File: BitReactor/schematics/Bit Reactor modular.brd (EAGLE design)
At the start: 100 x 50 mm, 111 parts, among them U1 ADC0808N, U2 4053D, U3 4053D, U4 741G3157DBVR, U5 TL072D, U6 LM3914N, U7 LM555D, U9 TL072D

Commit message: v1.2 from Ryan
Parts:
- removed JP1: (no value), jumper:JP1
- removed R66: 50k, Rebel:POT-ALPS-RK09L1140
- removed U9: TL072D, linear:SO08
- added C15, C16: 10u, resistor:E2-5
- added C17: 0.01uF, resistor:C0402
- added IC1: TL074D, linear:SO14
- C1, C8: device rcl:E5-6 -> resistor:E2-5
- C4: value 220pF -> 470pF
- R1, R16, R18, R2, R3, R4, R5, R6, R7, R8: value 2.26k -> 20k
- R10, R14, R15: value 1.13k -> 10k; device resistor:R0805W -> resistor:R0805
- R11, R12, R13, R9: value 1.13k -> 10k
- R17: value 2.26k -> 2.7K
- R19, R21, R22, R23: value 2.26k -> 10K; device resistor:R0805 -> Rebel:POT-ALPS-RK09L1140
- R20: value 2.26k -> 50k; device resistor:R0805 -> Rebel:POT-ALPS-RK09L1140
- R34: device resistor:R0402 -> resistor:R0805
- R36: value 10k -> 100k
- R54: value 120k -> 10k; device resistor:R0402 -> resistor:R0805
- R62, R63: value POT-ALPS-RK09L1140 -> 120K; device Rebel:POT-ALPS-RK09L1140 -> resistor:R0402
- R64, R65: value POT-ALPS-RK09L1140 -> 120k; device Rebel:POT-ALPS-RK09L1140 -> resistor:R0402
- moved R65 67.6 mm to (1.59, 30.3), turned to 0 degrees
- moved R63 61.5 mm to (7.78, 20.0), turned to 0 degrees
- moved R18 57.2 mm to (44.5, 43.8), turned to 0 degrees
- moved R19 40.9 mm to (49.7, 12.3)
- moved R21 37.4 mm to (68.8, 12.3)
- moved R64 33.6 mm to (58.3, 41.0), turned to 0 degrees
- moved R20 31.7 mm to (49.7, 37.7)
- moved R17 27.8 mm to (43.0, 3.97), turned to 270 degrees
- moved R22 18.2 mm to (87.8, 25.0)
- moved R13 17.6 mm to (87.8, 9.68), turned to 90 degrees
- moved C11 16.3 mm to (91.0, 42.7)
- moved C7 14.3 mm to (87.3, 1.59), turned to 180 degrees
- moved R41 10.3 mm to (1.27, 19.5), turned to 90 degrees
- moved R23 10.2 mm to (68.8, 37.7), turned to 270 degrees
- moved R12 9.24 mm to (87.8, 38.3), turned to 90 degrees
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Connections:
- removed net N$64: R14.2, R7.1, U2.14
- removed net N$67: R23.1, U4.1
- removed net N$74: R56.1, R63.2
- new net N$68: C16.+, R34.2
- new net N$85: R15.1, R16.1, U2.14
- net +12V: now also IC1.4, R17.2, R22.1; no longer R62.3, R64.3, U9.8
- net -12V: now also IC1.11; no longer U9.4
- net CV2IN: now also IC1.8; no longer U9.1
- net GND: now also C16.-, C17.1, IC1.10, IC1.12, IC1.3, IC1.5, R19.3, R21.1, R22.3, R23.1; no longer R17.2, R18.2, R19.2, R20.2, R21.2, R22.2, R23.2, R62.1, R63.1, R64.1, R65.1, U9.3, U9.5
- net N$10: now also AUDIOIN.P$2, C15.+; no longer R10.2, R3.1, U3.15
- net N$11: now also C15.-, R36.2; no longer R11.2, R4.1, U3.14
- net N$12: now also R13.1, R14.2, U2.1; no longer R12.2, R5.1
- net N$13: now also R5.1; no longer R12.1
- net N$14: now also R4.1; no longer R11.1
- net N$15: now also R3.1; no longer R10.1
- net N$16: now also R2.1; no longer R9.1
- net N$17: now also R8.1; no longer R15.1
- net N$18: now also R21.2, R62.1; no longer R15.2, R16.1, R8.1
- net N$19: now also IC1.2, R62.2, R63.1; no longer R17.1, U2.13
- net N$20: now also R18.2, R20.1, R34.1; no longer R34.2, R66.1
- net N$21: now also R7.1; no longer R14.1
- net N$22: now also R6.1; no longer R13.1
- net N$23: now also IC1.1, R56.1, R63.2; no longer R18.1, U2.1
- net N$24: now also R12.1, R13.2, U3.14; no longer R19.1
- net N$25: now also R11.1, R12.2, U3.15; no longer R20.1
- net N$26: now also R10.1, R11.2, U3.4; no longer R21.1
- net N$27: now also R10.2, R9.1, U4.4; no longer R22.1
- net N$28: now also R9.2, U4.1; no longer U4.4
- net N$38: now also R18.1; no longer R34.1
- net N$40: now also R20.2, R20.3; no longer R66.2, R66.3
- net N$42: now also R23.2, R64.2; no longer AUDIOIN.P$2, R36.2
- net N$45: now also U1.6; no longer JP1.2
- net N$47: now also IC1.6, R64.1; no longer R53.2
- net N$48: now also R23.3; no longer R65.3
- net N$49: now also IC1.7, R53.2, R65.1; no longer JP1.1, U1.6
- net N$65: now also R14.1, R15.2, U2.13; no longer R13.2, R6.1
- net N$71: now also IC1.13; no longer U9.6
- net N$72: now also R19.2; no longer R62.2
- net N$73: now also IC1.14; no longer U9.7
- net N$75: now also R21.3; no longer R63.3
- net N$80: now also C17.2
- net N$81: now also IC1.9; no longer U9.2
- net N$83: now also R22.2; no longer R64.2
- net N$9: now also R17.1, R19.1; no longer R2.1, R9.2, U3.4
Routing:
- net N$19: track 15.5 -> 96.4 mm, vias 0 -> 3
- net N$9: track 87.0 -> 11.7 mm, vias 4 -> 0
- net N$74: track 71.6 -> 0.00 mm, vias 1 -> 0
- net N$12: track 86.3 -> 21.5 mm, vias 3 -> 0
- net N$24: track 13.3 -> 53.8 mm, vias 0 -> 2
- net N$27: track 6.30 -> 40.3 mm, vias 0 -> 2
- net N$42: track 37.1 -> 4.34 mm, vias 1 -> 0
- net N$11: track 51.1 -> 20.7 mm, vias 2 -> 1
- net N$17: track 2.64 -> 31.3 mm, vias 0 -> 2
- net N$85: track 0.00 -> 28.4 mm
- net N$64: track 27.8 -> 0.00 mm
- net N$14: track 2.56 -> 27.4 mm
- net N$10: track 47.5 -> 24.0 mm, vias 2 -> 0
- net N$18: track 26.4 -> 3.29 mm
- net N$13: track 4.67 -> 24.4 mm
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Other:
- board text added: "C1"
- board text added: "C15"
- board text added: "C16"
- board text added: "C17"
- board text added: "C8"
- board text added: "D5"
- board text added: "R30"
- board text added: "R62"
- board text added: "R63"
- board text added: "R64"
- board text added: "R65"
- board text removed: "D6"

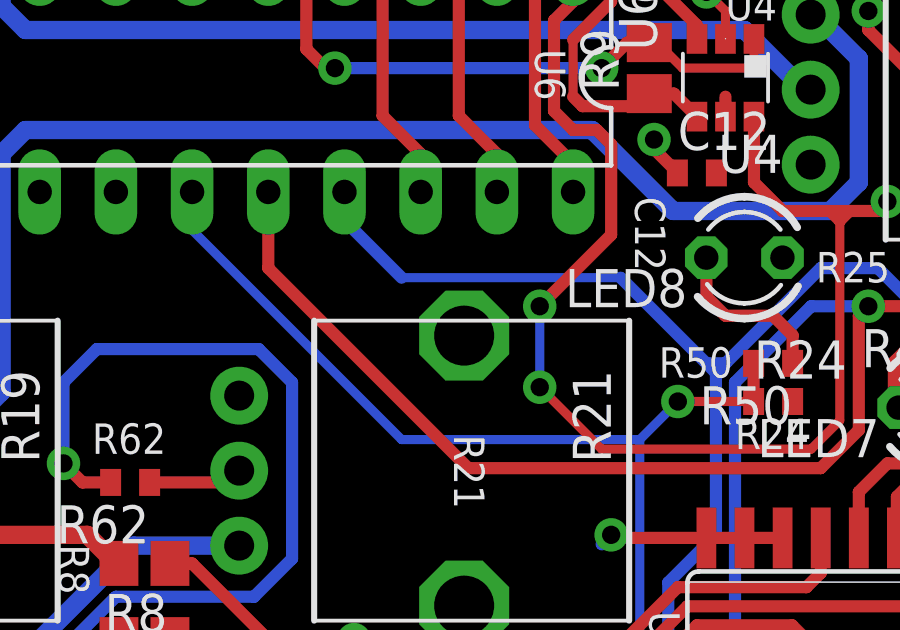
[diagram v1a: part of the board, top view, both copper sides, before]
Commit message: tied pot shells to gnd
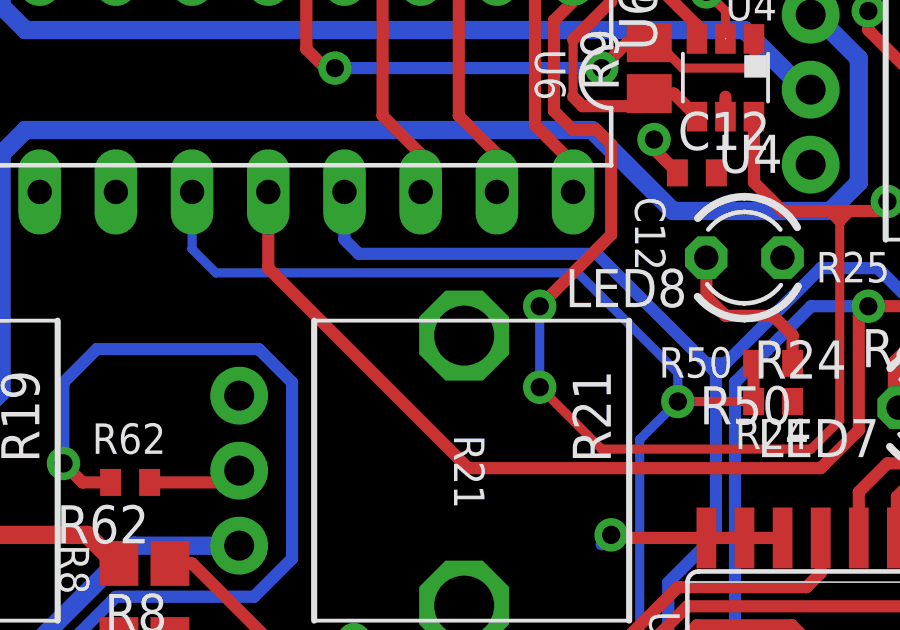
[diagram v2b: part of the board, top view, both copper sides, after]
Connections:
- net GND: now also R19.P$5, R19.P$6, R20.P$5, R20.P$6, R21.P$5, R21.P$6, R22.P$5, R22.P$6, R23.P$5, R23.P$6
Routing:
- net N$37: track 41.4 -> 43.1 mm
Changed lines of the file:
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@@
 <wire x1="2.68375" y1="20.47875" x2="2.69875" y2="20.47875" width="0.3048" layer="1"/>
 <wire x1="10.13" y1="26.05" x2="9.68375" y2="26.05" width="0.254" layer="1"/>
+<contactref element="R22" pad="P$5"/>
+<contactref element="R22" pad="P$6"/>
+<contactref element="R23" pad="P$5"/>
+<contactref element="R23" pad="P$6"/>
+<contactref element="R20" pad="P$5"/>
+<contactref element="R20" pad="P$6"/>
+<contactref element="R19" pad="P$5"/>
+<contactref element="R19" pad="P$6"/>
+<contactref element="R21" pad="P$5"/>
+<contactref element="R21" pad="P$6"/>
 </signal>
 <signal name="N$1">
@@
 <wire x1="77.1525" y1="10.16" x2="75.565" y2="8.5725" width="0.4064" layer="16"/>
 <wire x1="82.55" y1="19.05" x2="80.645" y2="19.05" width="0.4064" layer="16"/>
-<wire x1="64.77" y1="21.59" x2="64.77" y2="20.6375" width="0.4064" layer="16"/>
-<wire x1="64.77" y1="20.6375" x2="66.675" y2="18.7325" width="0.4064" layer="16"/>
-<wire x1="66.675" y1="18.7325" x2="73.9775" y2="18.7325" width="0.3048" layer="16"/>
-<wire x1="73.9775" y1="18.7325" x2="76.835" y2="15.875" width="0.4064" layer="16"/>
+<wire x1="73.18375" y1="19.52625" x2="76.835" y2="15.875" width="0.4064" layer="16"/>
 <wire x1="76.835" y1="15.875" x2="77.1525" y2="15.5575" width="0.4064" layer="16"/>
 <wire x1="76.835" y1="15.875" x2="77.47" y2="15.875" width="0.4064" layer="16"/>
+<wire x1="64.77" y1="21.59" x2="64.77" y2="20.0025" width="0.4064" layer="16"/>
+<wire x1="64.77" y1="20.0025" x2="65.24625" y2="19.52625" width="0.4064" layer="16"/>
+<wire x1="65.24625" y1="19.52625" x2="73.18375" y2="19.52625" width="0.4064" layer="16"/>
 </signal>
 <signal name="N$36">
@@
 <via x="75.8825" y="14.605" extent="1-16" drill="0.6096"/>
 <wire x1="75.8825" y1="14.605" x2="78.4075" y2="14.605" width="0.3048" layer="1"/>
-<wire x1="59.69" y1="21.59" x2="59.69" y2="20.32" width="0.3048" layer="16"/>
-<wire x1="59.69" y1="20.32" x2="66.675" y2="13.335" width="0.3048" layer="16"/>
-<wire x1="66.675" y1="13.335" x2="74.6125" y2="13.335" width="0.3048" layer="16"/>
 <wire x1="78.4075" y1="15.875" x2="78.4075" y2="14.62" width="0.4064" layer="1"/>
 <wire x1="78.4075" y1="14.62" x2="78.4225" y2="14.605" width="0.4064" layer="1"/>
 <wire x1="78.4075" y1="14.605" x2="78.4225" y2="14.605" width="0.4064" layer="1"/>
+<wire x1="59.69" y1="21.59" x2="59.69" y2="19.685" width="0.3048" layer="16"/>
+<wire x1="59.69" y1="19.685" x2="60.48375" y2="18.89125" width="0.3048" layer="16"/>
+<wire x1="60.48375" y1="18.89125" x2="72.54875" y2="18.89125" width="0.3048" layer="16"/>
+<wire x1="72.54875" y1="18.89125" x2="75.8825" y2="15.5575" width="0.3048" layer="16"/>
+<wire x1="75.8825" y1="15.5575" x2="75.8825" y2="14.605" width="0.3048" layer="16"/>
 </signal>
 <signal name="Y">

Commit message: v1.3
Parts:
- added C18: 10u, resistor:E2-5
- R17: value 2.7K -> 3.3K
- moved D1 0.95 mm to (24.1, 5.40)
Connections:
- net GND: now also C18.-
- net N$51: now also C18.+
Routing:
- net N$51: track 27.2 -> 29.8 mm
- net GND: track 129.7 -> 132.0 mm
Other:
- board text added: "Bit Reactor v1.3"
- board text added: "C18"
- board text added: "Rebel Technology"
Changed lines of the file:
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@@
 <?xml version="1.0" encoding="utf-8"?>
 <!DOCTYPE eagle SYSTEM "eagle.dtd">
-<eagle version="6.1">
+<eagle version="6.5.0">
 <drawing>
 <settings>
@@
 <setting verticaltext="up"/>
 </settings>
-<grid distance="0.00625" unitdist="inch" unit="inch" style="lines" multiple="1" display="no" altdistance="0.025" altunitdist="inch" altunit="inch"/>
+<grid distance="0.00625" unitdist="inch" unit="mm" style="lines" multiple="1" display="no" altdistance="0.025" altunitdist="inch" altunit="inch"/>
 <layers>
 <layer number="1" name="Top" color="4" fill="1" visible="yes" active="yes"/>
@@
 <text x="10.4775" y="16.35125" size="0.8128" layer="21" ratio="15" rot="SR0">R59</text>
 <text x="10.4775" y="19.52625" size="0.8128" layer="21" ratio="15" rot="SR0">R60</text>
-<text x="4.60375" y="16.98625" size="0.8128" layer="21" ratio="15" rot="SR0">R55</text>
+<text x="6.6675" y="16.1925" size="0.8128" layer="21" ratio="15" rot="SR0">R55</text>
 <text x="4.60375" y="18.7325" size="0.8128" layer="21" ratio="15" rot="SR0">R56</text>
 <text x="77.7875" y="13.0175" size="1.016" layer="21" ratio="15" rot="SR0">R24</text>
@@
 <text x="47.3075" y="19.3675" size="1.016" layer="21" ratio="15" rot="SR0">D4</text>
 <text x="43.18" y="48.73625" size="1.016" layer="21" ratio="15" rot="SR0">D5</text>
-<text x="21.9075" y="2.06375" size="1.016" layer="21" ratio="15" rot="SR0">D1</text>
+<text x="23.495" y="1.11125" size="1.016" layer="21" ratio="15" rot="SR0">D1</text>
 <text x="33.81375" y="0" size="1.016" layer="21" ratio="15" rot="SR0">D2</text>
 <text x="38.735" y="0" size="1.016" layer="21" ratio="15" rot="SR0">D3</text>
@@
 <text x="41.75125" y="0.79375" size="1.016" layer="21" ratio="15" rot="SR0">R17</text>
 <text x="45.56125" y="44.92625" size="1.016" layer="21" ratio="15" rot="SR0">R18</text>
-<text x="8.5725" y="46.51375" size="1.27" layer="22" rot="MR0">C1</text>
-<text x="21.59" y="24.92375" size="1.27" layer="22" rot="MR0">C16</text>
-<text x="10.16" y="34.6075" size="1.27" layer="22" rot="MR0">C15</text>
-<text x="42.545" y="7.46125" size="1.27" layer="22" rot="MR0">C8</text>
+<text x="8.5725" y="46.51375" size="1.27" layer="22" ratio="15" rot="MR0">C1</text>
+<text x="21.59" y="24.92375" size="1.27" layer="22" ratio="15" rot="MR0">C16</text>
+<text x="10.16" y="34.6075" size="1.27" layer="22" ratio="15" rot="MR0">C15</text>
+<text x="42.545" y="7.46125" size="1.27" layer="22" ratio="15" rot="MR0">C8</text>
 <text x="49.37125" y="13.335" size="1.016" layer="21" ratio="15" rot="SR270">R19</text>
 <text x="68.42125" y="13.49375" size="1.016" layer="21" ratio="15" rot="SR270">R21</text>
@@
 <text x="2.69875" y="29.845" size="0.8128" layer="21" ratio="15" rot="SR0">R65</text>
 <text x="6.82625" y="20.6375" size="0.8128" layer="21" ratio="15" rot="SR0">R63</text>
+<text x="25.4" y="5.3975" size="1.27" layer="22" ratio="15" rot="MR0">C18</text>
+<text x="97.5" y="48.26" size="1.016" layer="21" ratio="15" rot="SR270">Bit Reactor v1.3</text>
+<wire x1="95" y1="11" x2="95" y2="9" width="0.254" layer="21"/>
+<wire x1="94" y1="10" x2="96" y2="10" width="0.254" layer="21"/>
+<circle x="95" y="10" radius="1.209003125" width="0.3048" layer="21"/>
+<text x="97.5" y="15.24" size="1.016" layer="21" ratio="15" rot="SR270">Rebel Technology</text>
 </plain>
 <attributes>
@@
 </class>
 </classes>
-<designrules>
+<designrules name="SparkFun">
 <description language="en">&lt;b&gt;EAGLE Design Rules&lt;/b&gt;
 &lt;p&gt;
@@
 <element name="R54" library="resistor" package="R0805" value="10k" x="57.30875" y="32.0675"/>
 <element name="R58" library="resistor" package="R0402" value="120k" x="3.33375" y="19.05"/>
-<element name="D1" library="diode" package="SMA" value="MBRA340T3" x="24.13" y="6.35" rot="R270"/>
+<element name="D1" library="diode" package="SMA" value="MBRA340T3" x="24.13" y="5.3975" rot="R270"/>
 <element name="U$2" library="SparkFun" package="2X8" value="M08X2" x="2.54" y="2.2225"/>
 <element name="C8" library="resistor" package="E2-5" value="10u" x="38.1" y="9.68375" rot="MR180"/>
@@
 <element name="C16" library="resistor" package="E2-5" value="10u" x="19.52625" y="28.8925" rot="MR90"/>
 <element name="C15" library="resistor" package="E2-5" value="10u" x="11.43" y="32.0675" rot="MR270"/>
-<element name="R17" library="resistor" package="R0805" value="2.7K" x="43.02125" y="3.96875" rot="R270"/>
+<element name="R17" library="resistor" package="R0805" value="3.3K" x="43.02125" y="3.96875" rot="R270"/>
 <element name="IC1" library="linear" package="SO14" value="TL074D" x="4.60375" y="25.4" rot="R180"/>
 <element name="R62" library="resistor" package="R0402" value="120K" x="57.62625" y="11.90625" rot="R180"/>
@@
 <element name="R65" library="resistor" package="R0402" value="120k" x="1.5875" y="30.32125"/>
 <element name="C17" library="resistor" package="C0402" value="0.01uF" x="60.96" y="31.59125" rot="R180"/>
+<element name="C18" library="resistor" package="E2-5" value="10u" x="23.8125" y="9.525" rot="MR180"/>
 </elements>
 <signals>
@@
 <wire x1="39.055" y1="48.2575" x2="39.0525" y2="48.26" width="0.4064" layer="1"/>
 <wire x1="34.6075" y1="6.1275" x2="39.37" y2="6.1275" width="0.8128" layer="1"/>
-<wire x1="24.13" y1="4.35" x2="24.13" y2="2.2225" width="0.6096" layer="1"/>
-<via x="24.13" y="2.2225" extent="1-16" drill="0.6096"/>
-<wire x1="24.13" y1="2.2225" x2="24.13" y2="1.905" width="0.6096" layer="16"/>
+<via x="22.38375" y="1.74625" extent="1-16" drill="0.6096"/>
+<wire x1="22.38375" y1="1.74625" x2="24.13" y2="1.905" width="0.6096" layer="16"/>
 <wire x1="24.13" y1="1.905" x2="23.8125" y2="1.5875" width="0.6096" layer="16"/>
 <contactref element="C9" pad="1"/>
@@
 <contactref element="R21" pad="P$5"/>
 <contactref element="R21" pad="P$6"/>
+<contactref element="C18" pad="-"/>
+<wire x1="24.13" y1="3.3975" x2="23.0825" y2="3.3975" width="0.6096" layer="1"/>
+<wire x1="23.0825" y1="3.3975" x2="22.38375" y2="2.69875" width="0.6096" layer="1"/>
+<wire x1="22.38375" y1="2.69875" x2="22.38375" y2="1.74625" width="0.6096" layer="1"/>
 </signal>
 <signal name="N$1">
@@
 <wire x1="40.3225" y1="16.51" x2="39.0525" y2="15.24" width="0.6096" layer="1"/>
 <wire x1="46.355" y1="6.985" x2="47.625" y2="5.715" width="0.6096" layer="1"/>
-<wire x1="47.625" y1="5.715" x2="55.5625" y2="5.715" width="0.6096" layer="1"/>
 <wire x1="55.5625" y1="5.715" x2="56.515" y2="6.6675" width="0.6096" layer="1"/>
 <wire x1="56.515" y1="6.6675" x2="57.2525" y2="6.6675" width="0.6096" layer="1"/>
+<wire x1="47.625" y1="5.715" x2="55.5625" y2="5.715" width="0.6096" layer="1"/>
 </signal>
 <signal name="N$7">
@@
 <contactref element="F1" pad="1"/>
 <wire x1="15.24" y1="2.2225" x2="15.24" y2="4.7625" width="0.8128" layer="1"/>
-<via x="26.3525" y="9.2075" extent="1-16" drill="0.6096"/>
+<via x="27.78125" y="9.36625" extent="1-16" drill="0.6096"/>
 <wire x1="15.24" y1="2.2225" x2="15.24" y2="1.27" width="0.6096" layer="16"/>
 <wire x1="15.24" y1="1.27" x2="15.875" y2="0.635" width="0.6096" layer="16"/>
 <wire x1="15.875" y1="0.635" x2="25.0825" y2="0.635" width="0.6096" layer="16"/>
 <wire x1="25.0825" y1="0.635" x2="26.3525" y2="1.905" width="0.6096" layer="16"/>
-<wire x1="26.3525" y1="1.905" x2="26.3525" y2="9.2075" width="0.6096" layer="16"/>
-<wire x1="27.788" y1="7.62" x2="27.788" y2="8.407" width="0.4064" layer="1"/>
-<wire x1="27.788" y1="8.407" x2="26.9875" y2="9.2075" width="0.4064" layer="1"/>
-<wire x1="26.9875" y1="9.2075" x2="26.3525" y2="9.2075" width="0.4064" layer="1"/>
+<wire x1="27.788" y1="7.62" x2="27.788" y2="9.3595" width="0.4064" layer="1"/>
+<wire x1="27.788" y1="9.3595" x2="27.78125" y2="9.36625" width="0.4064" layer="1"/>
+<wire x1="26.3525" y1="1.905" x2="26.3525" y2="8.5725" width="0.6096" layer="16"/>
+<wire x1="26.3525" y1="8.5725" x2="27.14625" y2="9.36625" width="0.6096" layer="16"/>
+<wire x1="27.14625" y1="9.36625" x2="27.78125" y2="9.36625" width="0.6096" layer="16"/>
 </signal>
 <signal name="N$51">
@@
 <contactref element="U$2" pad="10"/>
 <wire x1="12.7" y1="2.2225" x2="12.7" y2="4.7625" width="0.8128" layer="1"/>
-<wire x1="26.035" y1="6.35" x2="27.6225" y2="4.7625" width="0.4064" layer="1"/>
 <wire x1="27.788" y1="4.7625" x2="27.6225" y2="4.7625" width="0.4064" layer="1"/>
 <wire x1="12.7" y1="4.7625" x2="12.7" y2="6.985" width="0.4064" layer="1"/>
@@
 <wire x1="17.4625" y1="11.43" x2="20.6375" y2="11.43" width="0.4064" layer="1"/>
 <wire x1="20.6375" y1="11.43" x2="21.59" y2="10.4775" width="0.4064" layer="1"/>
-<wire x1="21.59" y1="10.4775" x2="21.59" y2="7.3025" width="0.4064" layer="1"/>
-<wire x1="21.59" y1="7.3025" x2="22.5425" y2="6.35" width="0.4064" layer="1"/>
-<wire x1="22.5425" y1="6.35" x2="26.035" y2="6.35" width="0.4064" layer="1"/>
+<wire x1="21.59" y1="10.4775" x2="21.59" y2="10.00125" width="0.4064" layer="1"/>
+<contactref element="C18" pad="+"/>
+<wire x1="21.59" y1="10.00125" x2="21.59" y2="9.04875" width="0.4064" layer="1"/>
+<wire x1="21.59" y1="9.04875" x2="21.59" y2="6.82625" width="0.4064" layer="1"/>
+<wire x1="21.59" y1="6.82625" x2="22.86" y2="5.55625" width="0.4064" layer="1"/>
+<wire x1="22.86" y1="5.55625" x2="26.99425" y2="5.55625" width="0.4064" layer="1"/>
+<wire x1="26.99425" y1="5.55625" x2="27.788" y2="4.7625" width="0.4064" layer="1"/>
+<wire x1="22.06625" y1="9.525" x2="21.59" y2="10.00125" width="0.4064" layer="1"/>
+<wire x1="21.59" y1="9.04875" x2="22.06625" y2="9.525" width="0.4064" layer="1"/>
+<wire x1="22.06625" y1="9.525" x2="22.7965" y2="9.525" width="0.4064" layer="1"/>
 </signal>
 <signal name="N$70">
